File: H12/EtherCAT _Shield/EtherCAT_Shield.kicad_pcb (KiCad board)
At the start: 2 copper layers, 31 parts, among them J1 Conn_02x15_Odd_Even, J2 Conn_02x10_Odd_Even, J4 Conn_02x17_Odd_Even, J5 Conn_02x08_Odd_Even, SW1 RESET, U1 LAN9252I/PT, U2 24AA64T-E/OT, Y1 Crystal

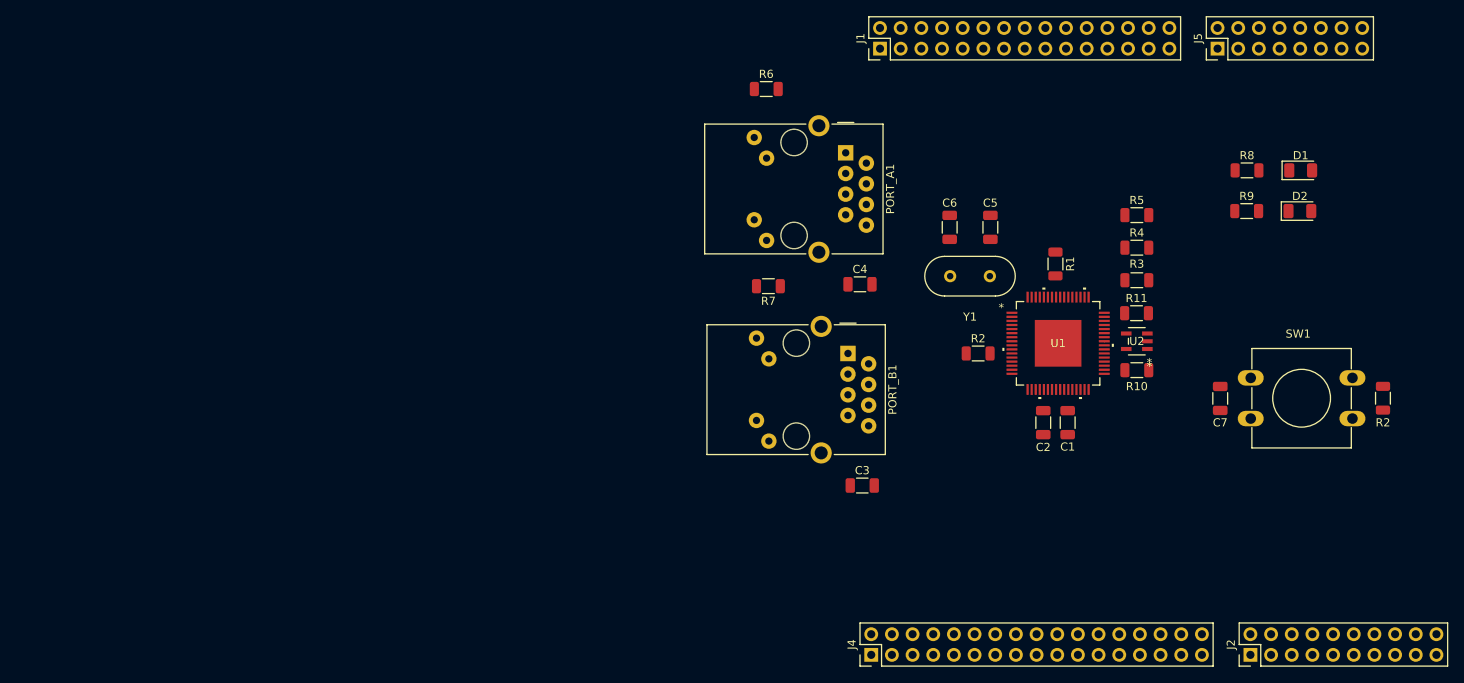
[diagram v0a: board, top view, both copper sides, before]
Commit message: PCB Resizing and component placement
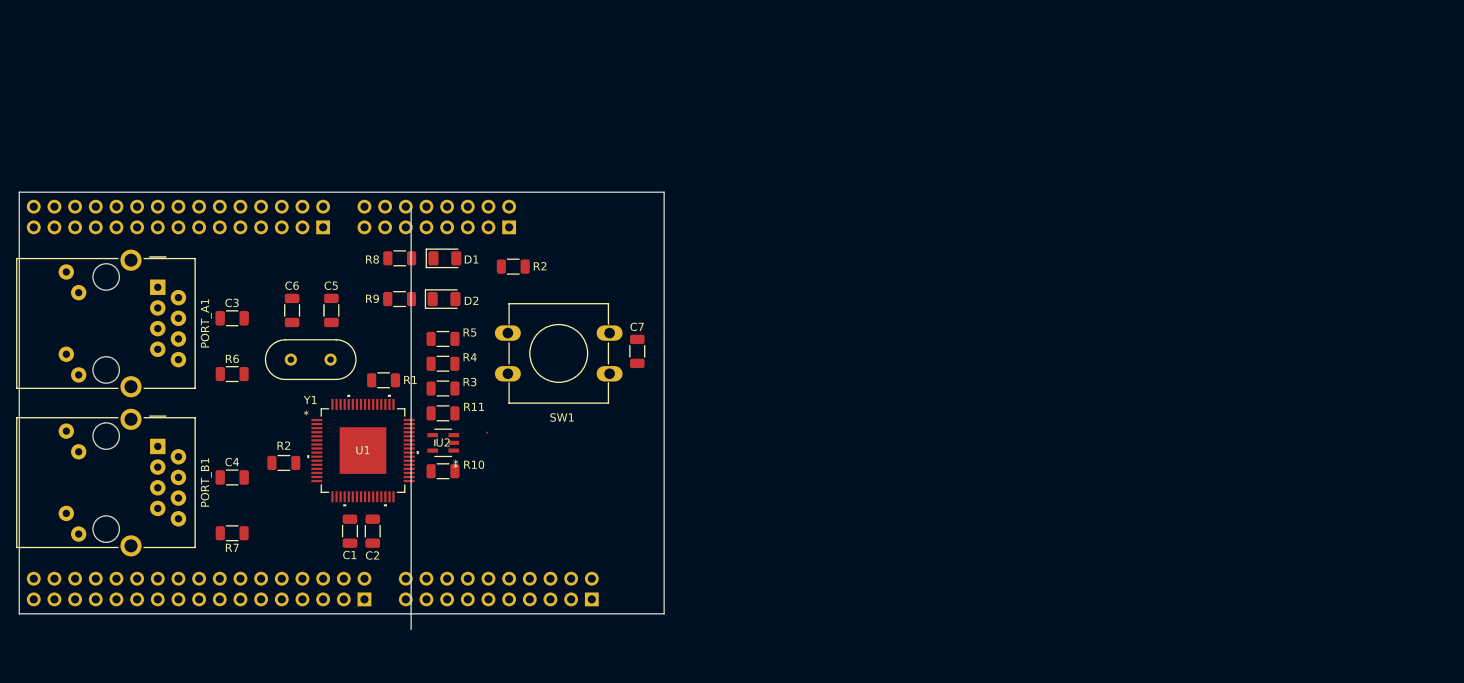
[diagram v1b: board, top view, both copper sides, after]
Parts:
- J1, J2, J4, J5: moved to B.Cu
- moved R2 108.1 mm to (86.9, 68.3), turned to 0 degrees
- moved D2 105.7 mm to (78.4, 72.3)
- moved D1 105.7 mm to (78.5, 67.3)
- moved R8 104.7 mm to (72.9, 67.3)
- moved R9 104.7 mm to (72.9, 72.3)
- moved J5 89.8 mm to (86.4, 63.5)
- moved C1 89.2 mm to (66.8, 100.8)
- moved R5 86.6 mm to (78.2, 77.2)
- moved R4 86.5 mm to (78.2, 80.3)
- moved U1 86.4 mm to (68.4, 90.9)
- moved R2 86.4 mm to (58.7, 92.5)
- moved R3 86.3 mm to (78.2, 83.3)
- moved R10 86.2 mm to (78.2, 93.5)
- moved U2 86.2 mm to (78.3, 90.0)
- moved PORT_A1 86.1 mm to (43.2, 70.9)
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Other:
- board outline added: 79.2 x 53.7 mm
